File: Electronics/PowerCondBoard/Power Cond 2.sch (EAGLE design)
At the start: 53 parts

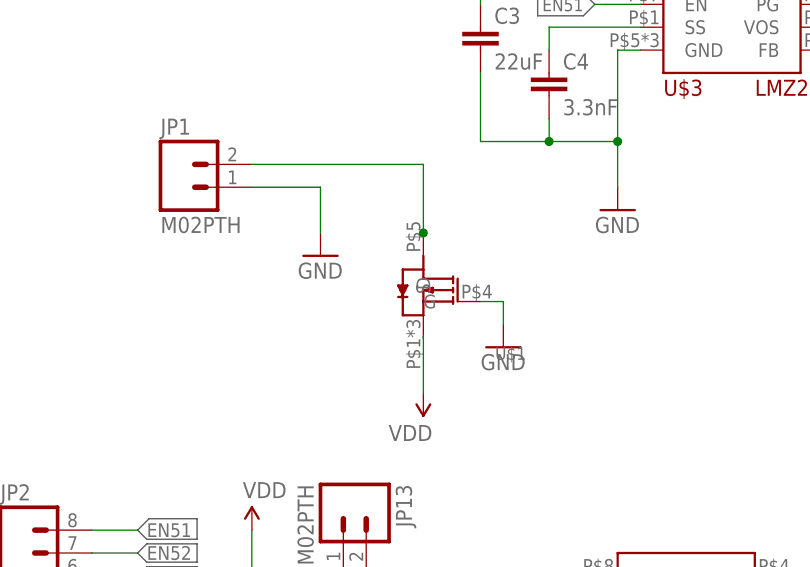
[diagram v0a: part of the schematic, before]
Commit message: P channel Fet and Power Cond Board
MTD20P03HDL with package DPAK_369C p channel fet was added to the lib
and placed on the Power Cond Board Schem
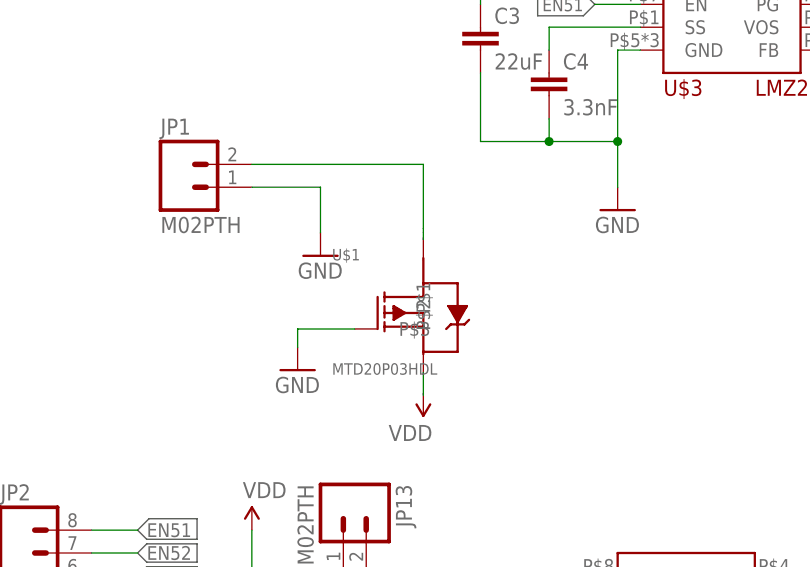
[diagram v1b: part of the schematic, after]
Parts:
- U$1: value SI7463ADP -> MTD20P03HDL; device RitLaunchInitiative:SI7463ADP -> RitLaunchInitiative:MTD20P03HDL
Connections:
- net GND: now also U$1.P$3; no longer U$1.G
- net N$1: no longer U$1.D
- net VDD: no longer U$1.S
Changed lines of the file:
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@@
 </classes>
 <parts>
-<part name="U$1" library="RitLaunchInitiative" deviceset="SI7463ADP" device=""/>
 <part name="U$2" library="RitLaunchInitiative" deviceset="LMZ21701" device=""/>
 <part name="U$3" library="RitLaunchInitiative" deviceset="LMZ21701" device=""/>
@@
 <part name="GND22" library="SparkFun-Aesthetics" deviceset="GND" device=""/>
 <part name="GND23" library="SparkFun-Aesthetics" deviceset="GND" device=""/>
+<part name="U$1" library="RitLaunchInitiative" deviceset="MTD20P03HDL" device=""/>
 </parts>
 <sheets>
@@
 </plain>
 <instances>
-<instance part="U$1" gate="G$1" x="-10.16" y="-2.54" smashed="yes" rot="R180">
-<attribute name="NAME" x="0" y="-10.16" size="1.397" layer="95" rot="R180"/>
-</instance>
 <instance part="U$2" gate="G$1" x="22.86" y="73.66"/>
 <instance part="U$3" gate="G$1" x="22.86" y="25.4"/>
@@
 <instance part="JP2" gate="G$1" x="-53.34" y="-40.64"/>
 <instance part="JP1" gate="G$1" x="-38.1" y="7.62"/>
-<instance part="GND1" gate="1" x="-2.54" y="-10.16"/>
+<instance part="GND1" gate="1" x="-25.4" y="-12.7"/>
 <instance part="GND3" gate="1" x="-66.04" y="43.18"/>
 <instance part="R1" gate="G$1" x="43.18" y="63.5" rot="R90"/>
@@
 <instance part="GND22" gate="1" x="35.56" y="-116.84"/>
 <instance part="GND23" gate="1" x="2.54" y="-116.84"/>
+<instance part="U$1" gate="G$1" x="-11.43" y="-5.588"/>
 </instances>
 <busses>
@@
 <pinref part="JP1" gate="G$1" pin="2"/>
 <wire x1="-30.48" y1="10.16" x2="-11.43" y2="10.16" width="0.1524" layer="91"/>
-<pinref part="U$1" gate="G$1" pin="D"/>
-<wire x1="-11.43" y1="10.16" x2="-11.43" y2="2.54" width="0.1524" layer="91"/>
-<junction x="-11.43" y="2.54"/>
+<wire x1="-11.43" y1="10.16" x2="-11.43" y2="3.048" width="0.1524" layer="91"/>
+<wire x1="-11.43" y1="3.048" x2="-11.43" y2="2.54" width="0.1524" layer="91"/>
+<wire x1="-11.43" y1="1.778" x2="-11.43" y2="2.54" width="0.1524" layer="91"/>
 </segment>
 </net>
 <net name="GND" class="0">
-<segment>
-<pinref part="U$1" gate="G$1" pin="G"/>
-<wire x1="-5.08" y1="-5.08" x2="-2.54" y2="-5.08" width="0.1524" layer="91"/>
-<wire x1="-2.54" y1="-5.08" x2="-2.54" y2="-7.62" width="0.1524" layer="91"/>
-<pinref part="GND1" gate="1" pin="GND"/>
-</segment>
 <segment>
 <pinref part="JP1" gate="G$1" pin="1"/>
@@
 <pinref part="GND23" gate="1" pin="GND"/>
 </segment>
+<segment>
+<pinref part="U$1" gate="G$1" pin="P$3"/>
+<pinref part="GND1" gate="1" pin="GND"/>
+<wire x1="-19.05" y1="-8.128" x2="-25.4" y2="-8.128" width="0.1524" layer="91"/>
+<wire x1="-25.4" y1="-8.128" x2="-25.4" y2="-10.16" width="0.1524" layer="91"/>
+</segment>
 </net>
 <net name="EN51" class="0">
@@
 </net>
 <net name="VDD" class="0">
-<segment>
-<pinref part="U$1" gate="G$1" pin="S"/>
-<wire x1="-11.43" y1="-9.144" x2="-11.43" y2="-8.89" width="0.1524" layer="91"/>
-<wire x1="-11.43" y1="-9.144" x2="-11.43" y2="-15.24" width="0.1524" layer="91"/>
-<pinref part="SUPPLY1" gate="VDD" pin="VDD"/>
-</segment>
 <segment>
 <pinref part="SUPPLY4" gate="VDD" pin="VDD"/>
@@
 </segment>
 </net>
+<net name="N$4" class="0">
+<segment>
+<wire x1="-11.43" y1="-12.954" x2="-11.43" y2="-15.494" width="0.1524" layer="91"/>
+</segment>
+</net>

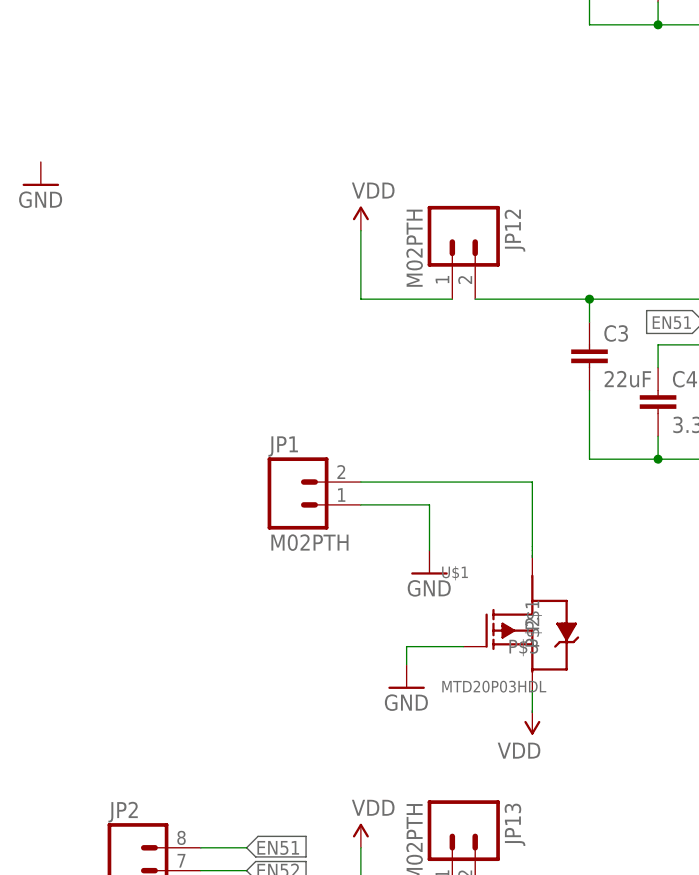
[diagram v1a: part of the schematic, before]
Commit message: changed the pin names in lbr
MTD20P03HDL has changed pin names
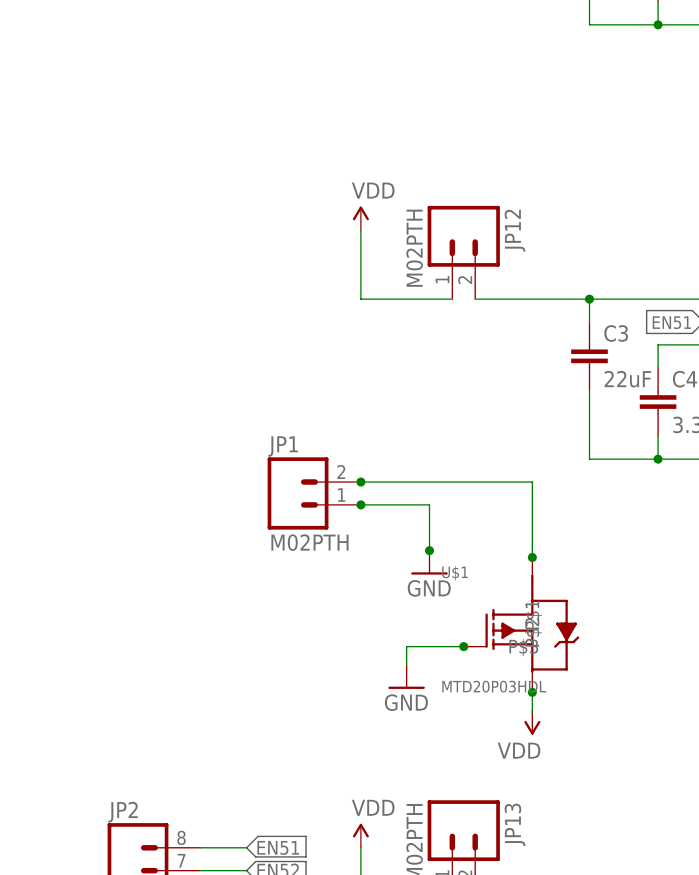
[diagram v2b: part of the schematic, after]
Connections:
- new net N$4: U$1.P$2
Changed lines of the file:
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@@
 <part name="JP1" library="SparkFun-Connectors" deviceset="M02" device="PTH"/>
 <part name="GND1" library="SparkFun-Aesthetics" deviceset="GND" device=""/>
-<part name="GND3" library="SparkFun-Aesthetics" deviceset="GND" device=""/>
 <part name="R1" library="SparkFun-Passives" deviceset="RESISTOR" device="0603-RES" value="180K"/>
 <part name="R2" library="SparkFun-Passives" deviceset="RESISTOR" device="0603-RES" value="1.02M"/>
@@
 <instance part="JP1" gate="G$1" x="-38.1" y="7.62"/>
 <instance part="GND1" gate="1" x="-25.4" y="-12.7"/>
-<instance part="GND3" gate="1" x="-66.04" y="43.18"/>
 <instance part="R1" gate="G$1" x="43.18" y="63.5" rot="R90"/>
 <instance part="R2" gate="G$1" x="50.8" y="71.12" rot="R180"/>
@@
 <instance part="GND22" gate="1" x="35.56" y="-116.84"/>
 <instance part="GND23" gate="1" x="2.54" y="-116.84"/>
-<instance part="U$1" gate="G$1" x="-11.43" y="-5.588"/>
+<instance part="U$1" gate="G$1" x="-11.43" y="-5.588" smashed="yes">
+<attribute name="NAME" x="-21.59" y="-0.508" size="1.27" layer="95"/>
+<attribute name="VALUE" x="-21.59" y="-13.208" size="1.27" layer="96"/>
+</instance>
 </instances>
 <busses>
@@
 <wire x1="-11.43" y1="3.048" x2="-11.43" y2="2.54" width="0.1524" layer="91"/>
 <wire x1="-11.43" y1="1.778" x2="-11.43" y2="2.54" width="0.1524" layer="91"/>
+<junction x="-11.43" y="1.778"/>
+<junction x="-30.48" y="10.16"/>
 </segment>
 </net>
@@
 <wire x1="-22.86" y1="7.62" x2="-22.86" y2="2.54" width="0.1524" layer="91"/>
 <pinref part="GND2" gate="1" pin="GND"/>
+<junction x="-22.86" y="2.54"/>
+<junction x="-30.48" y="7.62"/>
 </segment>
 <segment>
@@
 <wire x1="-19.05" y1="-8.128" x2="-25.4" y2="-8.128" width="0.1524" layer="91"/>
 <wire x1="-25.4" y1="-8.128" x2="-25.4" y2="-10.16" width="0.1524" layer="91"/>
+<junction x="-19.05" y="-8.128"/>
 </segment>
 </net>
@@
 <net name="N$4" class="0">
 <segment>
-<wire x1="-11.43" y1="-12.954" x2="-11.43" y2="-15.494" width="0.1524" layer="91"/>
-</segment>
-</net>
+<wire x1="-11.43" y1="-12.954" x2="-11.43" y2="-13.208" width="0.1524" layer="91"/>
+<pinref part="U$1" gate="G$1" pin="P$2"/>
+<junction x="-11.43" y="-13.208"/>
+<wire x1="-11.43" y1="-13.208" x2="-11.43" y2="-15.494" width="0.1524" layer="91"/>
+</segment>
+</net>
